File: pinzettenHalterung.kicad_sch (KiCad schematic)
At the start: 14 parts, among them J1 Conn_01x04_Pin, J3 Conn_01x02_Pin, J4 Conn_01x02_Pin, Q1 IRF740, Q2 BC546, Q3 BC546

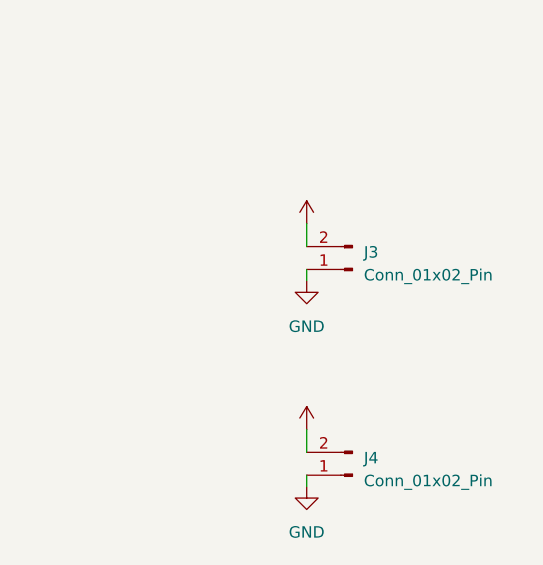
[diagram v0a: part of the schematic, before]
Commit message: change pin 01x02 to 01x03
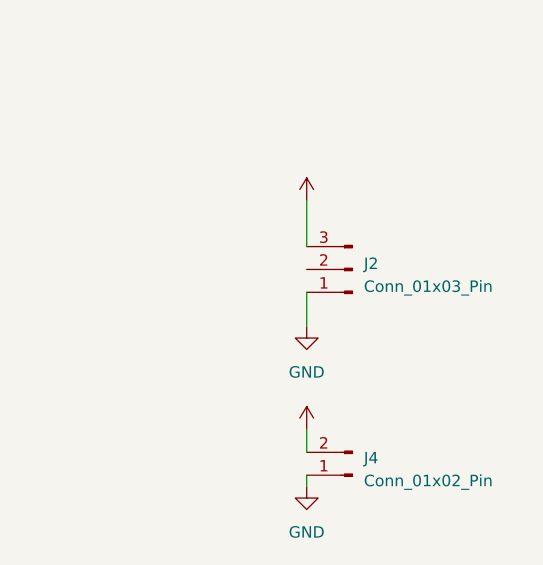
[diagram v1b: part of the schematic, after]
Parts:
- removed J3: Conn_01x02_Pin, symbol Connector:Conn_01x02_Pin
- added J2: Conn_01x03_Pin, symbol Connector:Conn_01x03_Pin
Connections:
- net GND: now also J2.1 (Pin_1)
- net VCC: now also J2.3 (Pin_3)
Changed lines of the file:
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@@
     (stroke (width 0) (type default))
   )
-  (wire (pts (xy 201.93 80.01) (xy 201.93 82.55))
+  (wire (pts (xy 201.93 77.47) (xy 201.93 82.55))
     (stroke (width 0) (type default))
   )
@@
     (stroke (width 0) (type default))
   )
-  (wire (pts (xy 201.93 85.09) (xy 201.93 86.36))
+  (wire (pts (xy 201.93 87.63) (xy 201.93 91.44))
     (stroke (width 0) (type default))
   )
@@
     )
   )
-  (symbol (lib_id "power:VCC") (at 201.93 80.01 0) (unit 1)
+  (symbol (lib_id "power:VCC") (at 201.93 77.47 0) (unit 1)
     (in_bom yes) (on_board yes) (dnp no)
-    (property "Reference" "#PWR06" (at 201.93 83.82 0)
-      (effects (font (size 1.27 1.27)) hide)
-    )
-    (property "Value" "VCC" (at 204.47 77.47 0)
-      (effects (font (size 1.27 1.27)) hide)
-    )
-    (property "Footprint" "" (at 201.93 80.01 0)
-      (effects (font (size 1.27 1.27)) hide)
-    )
-    (property "Datasheet" "" (at 201.93 80.01 0)
+    (property "Reference" "#PWR06" (at 201.93 81.28 0)
+      (effects (font (size 1.27 1.27)) hide)
+    )
+    (property "Value" "VCC" (at 204.47 74.93 0)
+      (effects (font (size 1.27 1.27)) hide)
+    )
+    (property "Footprint" "" (at 201.93 77.47 0)
+      (effects (font (size 1.27 1.27)) hide)
+    )
+    (property "Datasheet" "" (at 201.93 77.47 0)
       (effects (font (size 1.27 1.27)) hide)
     )
@@
     )
   )
-  (symbol (lib_id "power:GND") (at 201.93 86.36 0) (unit 1)
-    (in_bom yes) (on_board yes) (dnp no) (fields_autoplaced)
-    (property "Reference" "#PWR05" (at 201.93 92.71 0)
-      (effects (font (size 1.27 1.27)) hide)
-    )
-    (property "Value" "GND" (at 201.93 91.44 0)
-      (effects (font (size 1.27 1.27)))
-    )
-    (property "Footprint" "" (at 201.93 86.36 0)
-      (effects (font (size 1.27 1.27)) hide)
-    )
-    (property "Datasheet" "" (at 201.93 86.36 0)
+  (symbol (lib_id "power:GND") (at 201.93 91.44 0) (unit 1)
+    (in_bom yes) (on_board yes) (dnp no) (fields_autoplaced)
+    (property "Reference" "#PWR05" (at 201.93 97.79 0)
+      (effects (font (size 1.27 1.27)) hide)
+    )
+    (property "Value" "GND" (at 201.93 96.52 0)
+      (effects (font (size 1.27 1.27)))
+    )
+    (property "Footprint" "" (at 201.93 91.44 0)
+      (effects (font (size 1.27 1.27)) hide)
+    )
+    (property "Datasheet" "" (at 201.93 91.44 0)
       (effects (font (size 1.27 1.27)) hide)
     )
@@
     )
   )
-  (symbol (lib_id "Connector:Conn_01x02_Pin") (at 207.01 85.09 180) (unit 1)
-    (in_bom yes) (on_board yes) (dnp no) (fields_autoplaced)
-    (property "Reference" "J3" (at 208.28 83.185 0)
+  (symbol (lib_id "Connector:Conn_01x03_Pin") (at 207.01 85.09 180) (unit 1)
+    (in_bom yes) (on_board yes) (dnp no) (fields_autoplaced)
+    (property "Reference" "J2" (at 208.28 84.455 0)
       (effects (font (size 1.27 1.27)) (justify right))
     )
-    (property "Value" "Conn_01x02_Pin" (at 208.28 85.725 0)
+    (property "Value" "Conn_01x03_Pin" (at 208.28 86.995 0)
       (effects (font (size 1.27 1.27)) (justify right))
     )
@@
     (pin "1")
     (pin "2")
-    (instances
-      (project "pinzettenHalterung"
-        (path "/a11b48b6-91e4-44d4-a7dd-b589898b206a"
-          (reference "J3") (unit 1)
-        )
-      )
+    (pin "3")
+    (instances
+      (project "pinzettenHalterung"
+        (path "/a11b48b6-91e4-44d4-a7dd-b589898b206a"
+          (reference "J2") (unit 1)
+        )
+      )
